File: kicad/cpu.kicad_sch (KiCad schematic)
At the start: 13 parts, among them U3 74HC138, U4 W65C02SxP, U6 74HC04, U7 74HC00

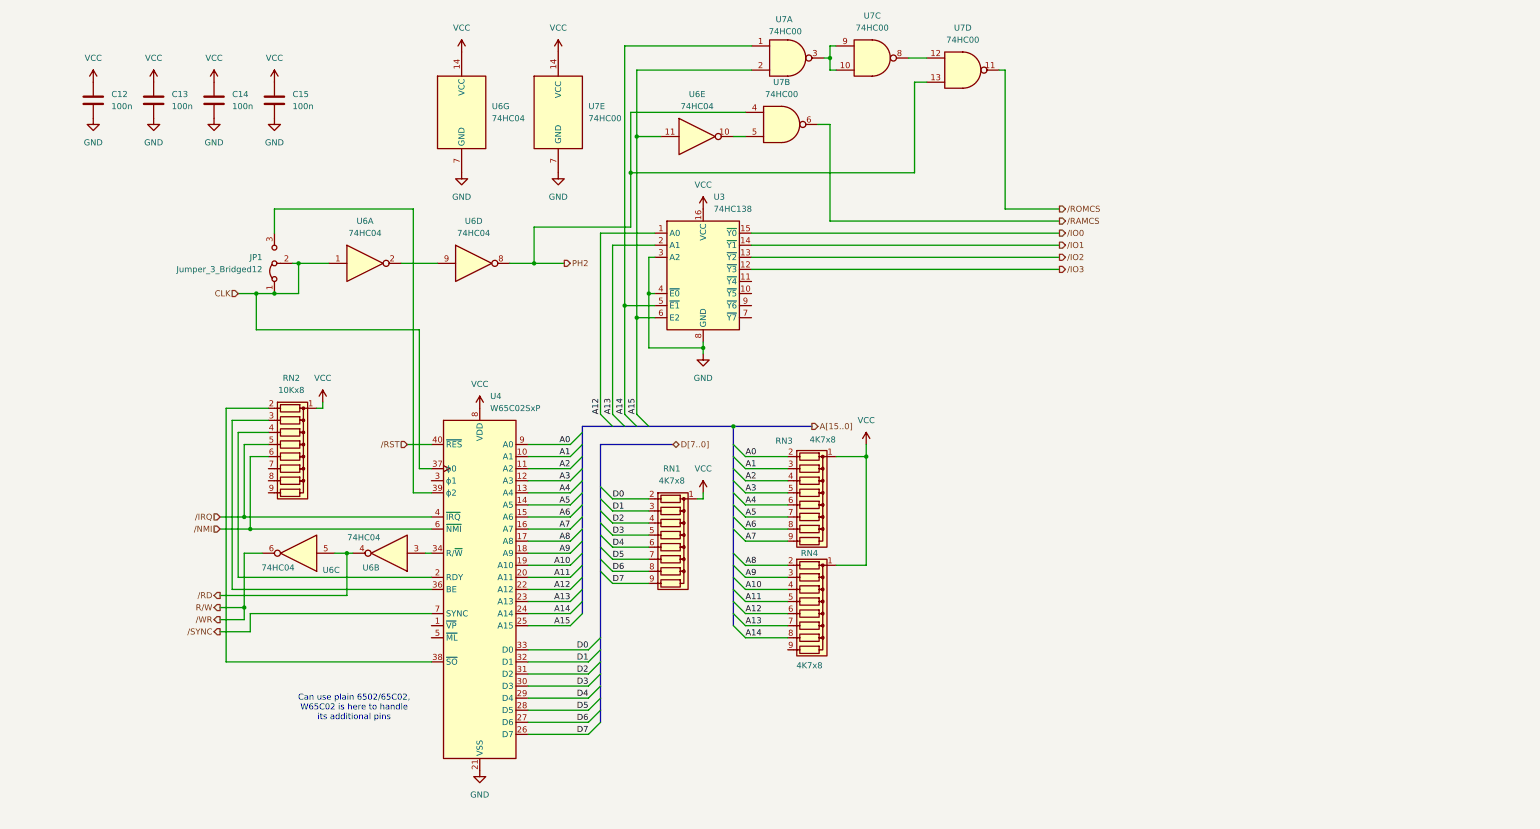
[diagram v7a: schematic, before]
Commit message: hw: revision C
Major changes:
- ROM space has been extended from 16 KiB to 32 KiB
- dynamic RAM option has been removed
- RAM size has been reduced from 32 KiB to 24 KiB
- expansion slot now replaces internal ROM, does not
  have dedicated memory space anymore
- place all I/O within a compactish 8 KiB
- move PH2 gating to /RD and /WR signals
- PCB redo (mechanicaly compatible)
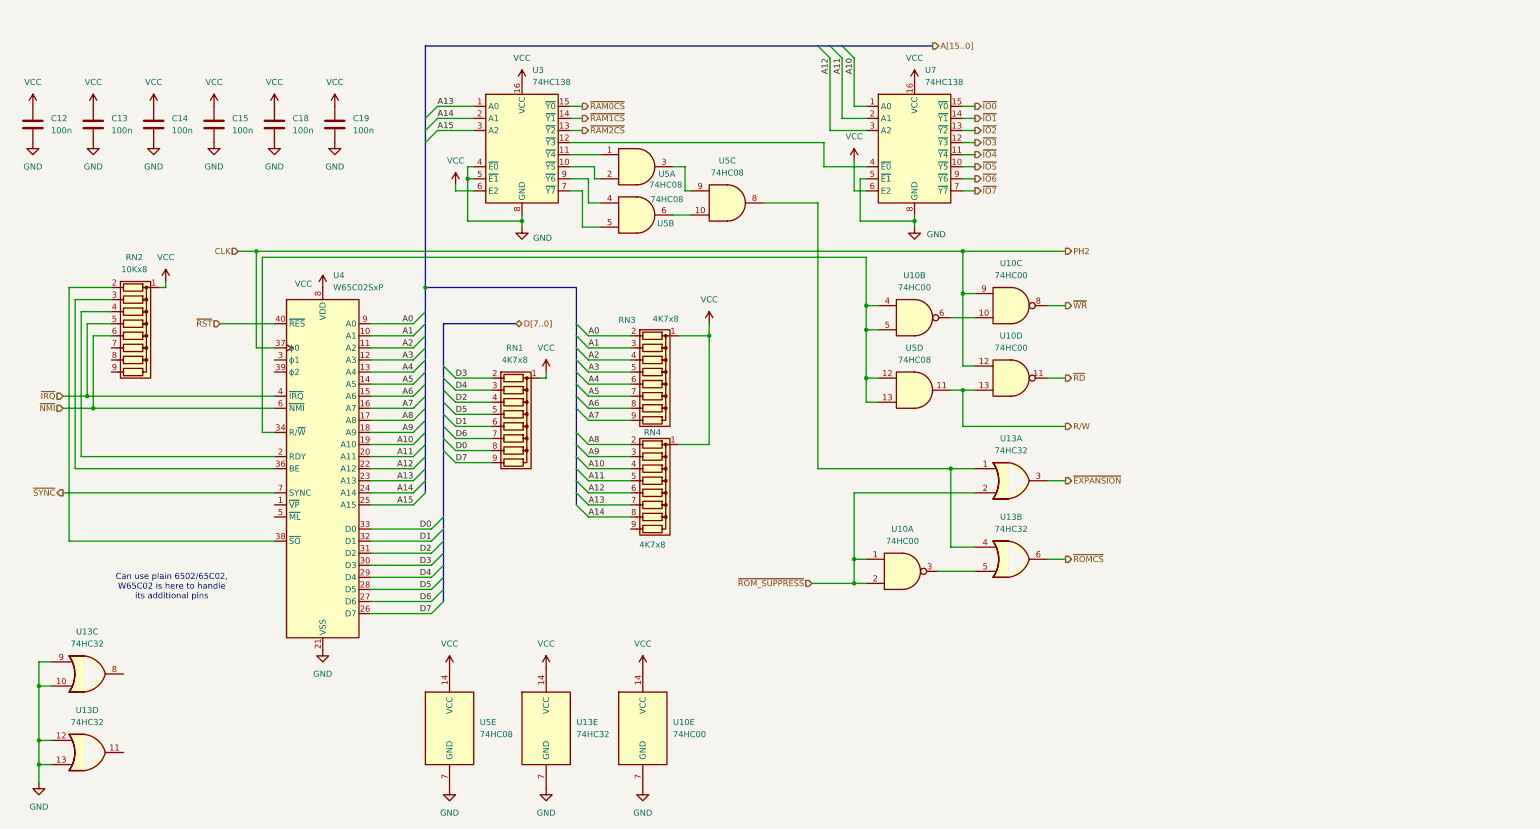
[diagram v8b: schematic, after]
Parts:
- removed JP1: Jumper_3_Bridged12, Jumper:SolderJumper-3_P1.3mm_Bridged12_Pad1.0x1.5mm, symbol Jumper:Jumper_3_Bridged12
- removed U6: 74HC04, Package_DIP:DIP-14_W7.62mm, symbol 74xx:74HC04
- removed U7: 74HC00, Package_DIP:DIP-14_W7.62mm, symbol 74xx:74HC00
- added C18, C19: 100n, Capacitor_THT:C_Disc_D5.0mm_W2.5mm_P2.50mm, symbol Device:C
- added U10: 74HC00, Package_DIP:DIP-14_W7.62mm, symbol 74xx:74HC00
- added U13: 74HC32, Package_DIP:DIP-14_W7.62mm, symbol 74xx:74LS32
- added U5: 74HC08, Package_DIP:DIP-14_W7.62mm, symbol 74xx:74LS08
- added U7: 74HC138, Package_DIP:DIP-16_W7.62mm, symbol 74xx:74HC138
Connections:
- net A10: now also U7.1 (A0)
- net A11: now also U7.2 (A1)
- net A12: now also U7.3 (A2); no longer U3.1 (A0)
- net A13: now also U3.1 (A0); no longer U3.2 (A1)
- net A14: now also U3.2 (A1); no longer U3.5 (~{E1})
- net A15: now also U3.3 (A2); no longer U3.6 (E2)
- net CLK: now also U10.12, U10.9
- net D0: now also RN1.8 (R7); no longer RN1.2 (R1)
- net D1: now also RN1.6 (R5); no longer RN1.3 (R2)
- net D3: now also RN1.2 (R1); no longer RN1.5 (R4)
- net D4: now also RN1.3 (R2); no longer RN1.6 (R5)
- net D5: now also RN1.5 (R4); no longer RN1.7 (R6)
- net D6: now also RN1.7 (R6); no longer RN1.8 (R7)
- net GND: now also U3.5 (~{E1}), C18.2, C19.2, U10.7 (GND), U13.10, U13.12, U13.13, U13.7 (GND), U13.9, U5.7 (GND), U7.5 (~{E1}), U7.8 (GND); no longer U3.3 (A2)
- net R/W: now also U10.13, U5.11
- net VCC: now also U3.6 (E2), C18.1, C19.1, U10.14 (VCC), U13.14 (VCC), U5.14 (VCC), U7.16 (VCC), U7.6 (E2)
- net at U4.34 (R/~{W}): now also U10.4, U10.5, U5.12, U5.13
- net at U3.10 (~{Y5}): now also U5.2
- net at U3.11 (~{Y4}): now also U5.1
- net at U3.7 (~{Y7}): now also U5.5
- net at U3.9 (~{Y6}): now also U5.4
- net /IO0 renamed ~{RAM0CS}
- net /IO1 renamed ~{RAM1CS}
- net /IO2 renamed ~{RAM2CS}
- net /IO3: no longer names the net of U3.12 (~{Y3})
- net /IO3: now also U7.4 (~{E0})
- net /IRQ renamed ~{IRQ}
- net /NMI renamed ~{NMI}
- net /RST renamed ~{RST}
- net /SYNC renamed ~{SYNC}
- new net: U5.10, U5.6
- new net: U10.10, U10.6
- new net: U5.3, U5.9
- new net: U13.1, U13.4, U5.8
- new net: U10.3, U13.5
- new net ~{EXPANSION}: U13.3
- new net ~{IO0}: U7.15 (~{Y0})
- new net ~{IO1}: U7.14 (~{Y1})
- new net ~{IO2}: U7.13 (~{Y2})
- new net ~{IO3}: U7.12 (~{Y3})
- new net ~{IO4}: U7.11 (~{Y4})
- new net ~{IO5}: U7.10 (~{Y5})
- new net ~{IO6}: U7.9 (~{Y6})
- new net ~{IO7}: U7.7 (~{Y7})
- new net ~{RD}: U10.11
- new net ~{ROMCS}: U13.6
- new net ~{ROM_SUPPRESS}: U10.1, U10.2, U13.2
- new net ~{WR}: U10.8
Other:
- moved on the sheet: C12, C13, C14, C15, RN1, RN2, RN3, RN4, U4
